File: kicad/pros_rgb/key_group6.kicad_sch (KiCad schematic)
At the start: 16 parts

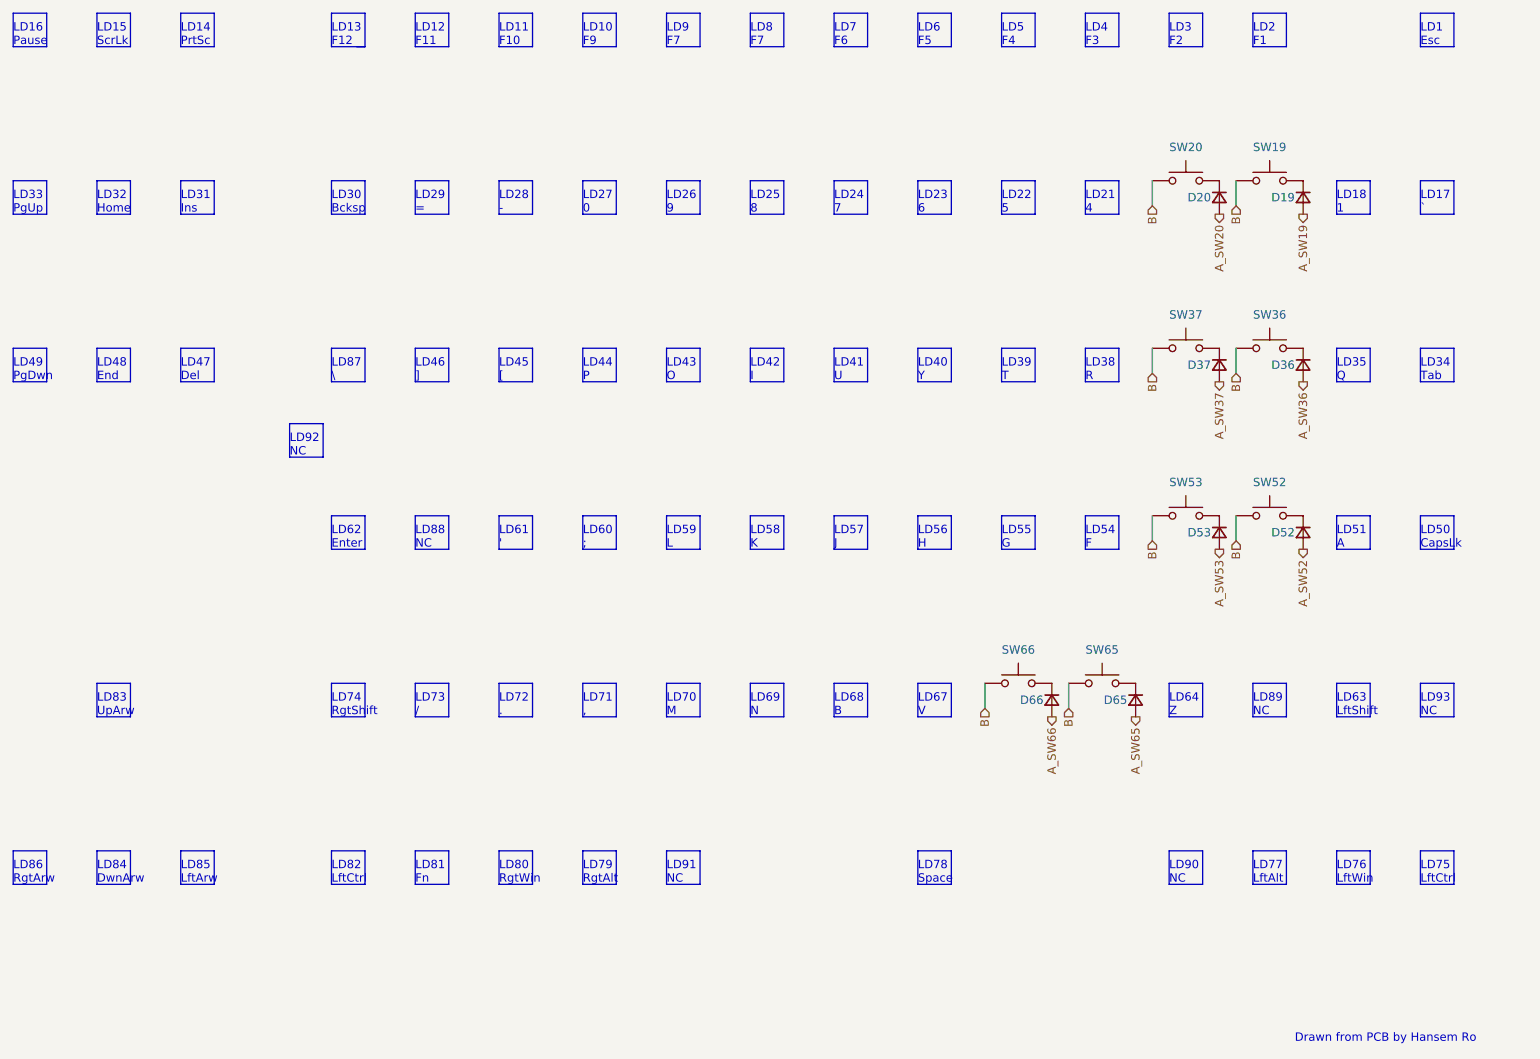
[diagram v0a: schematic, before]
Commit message: kicad/pros_rgb: update key groupings
These new groupings are based off ordering in firmware:
https://github.com/hansemro/pok3r_re_firmware/blob/4b68aa4baf7d28dc8dbf8eebcb1fdb59e7bcd629/disassemble/cmprosrgb/v122/cmprosrgb_v122.txt#L14599-L14629
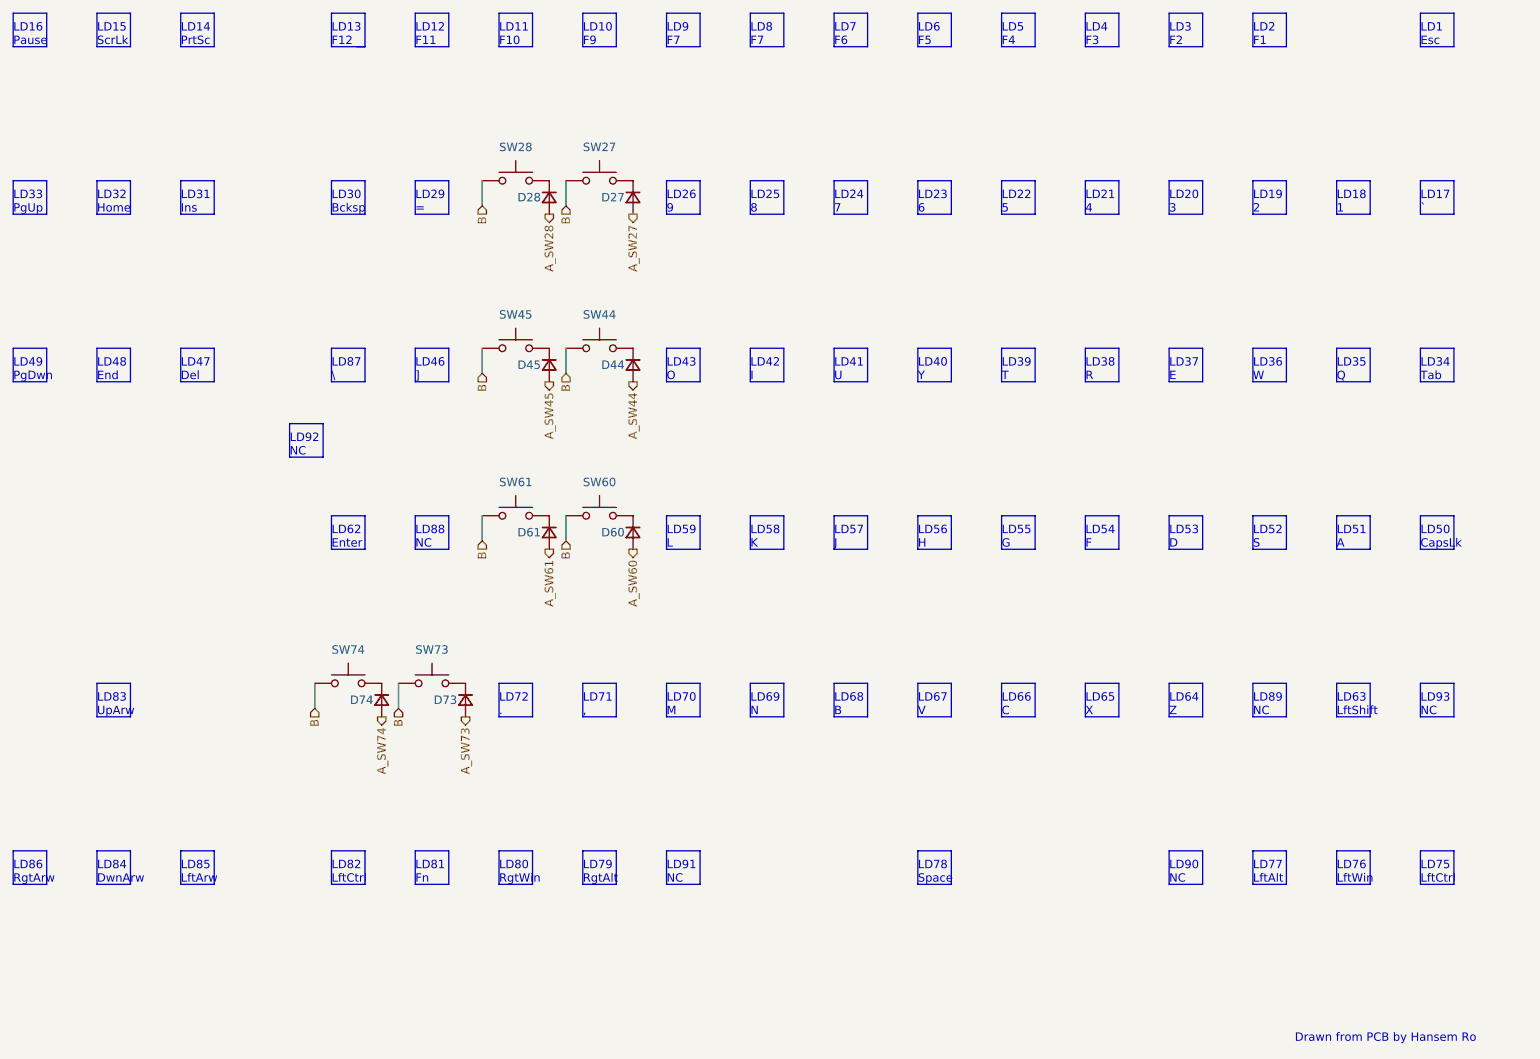
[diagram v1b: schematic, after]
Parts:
- removed D19, D20, D36, D37, D52, D53, D65, D66: ~, symbol Device:D_Small
- removed SW19, SW20, SW36, SW37, SW52, SW53, SW65, SW66: ~, symbol Switch:SW_Push
- added D27, D28, D44, D45, D60, D61, D73, D74: (no value), symbol Device:D_Small
- added SW27, SW28, SW44, SW45, SW60, SW61, SW73, SW74: (no value), symbol Switch:SW_Push
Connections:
- net B: now also SW27.1, SW28.1, SW44.1, SW45.1, SW60.1, SW61.1, SW73.1, SW74.1
- new net: D28.1 (K), SW28.2
- new net: D74.1 (K), SW74.2
- new net: D44.1 (K), SW44.2
- new net: D61.1 (K), SW61.2
- new net: D45.1 (K), SW45.2
- new net: D73.1 (K), SW73.2
- new net: D60.1 (K), SW60.2
- new net: D27.1 (K), SW27.2
- new net A_SW27: D27.2 (A)
- new net A_SW28: D28.2 (A)
- new net A_SW44: D44.2 (A)
- new net A_SW45: D45.2 (A)
- new net A_SW60: D60.2 (A)
- new net A_SW61: D61.2 (A)
- new net A_SW73: D73.2 (A)
- new net A_SW74: D74.2 (A)
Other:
- note added: "LD19 2"
- note added: "LD20 3"
- note added: "LD36 W"
- note added: "LD37 E"
- note added: "LD52 S"
- note added: "LD53 D"
- note added: "LD65 X"
- note added: "LD66 C"
- note removed: "LD27 0"
- note removed: "LD28 -"
- note removed: "LD44 P"
- note removed: "LD45 ["
- note removed: "LD60 ;"
- note removed: "LD61 '"
- note removed: "LD73 /"
- note removed: "LD74 RgtShift"

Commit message: kicad/pros_rgb: mark as Rev. B
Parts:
- D27, D28, D44, D45, D60, D61, D73, D74, SW27, SW28, SW44, SW45, SW60, SW61, SW73, SW74: value (none) -> ~
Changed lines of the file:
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@@
     (in_bom yes) (on_board yes)
     (property "Reference" "SW28" (id 0) (at 134.62 44.45 0))
-    (property "Value" "" (id 1) (at 134.62 44.45 0))
+    (property "Value" "~" (id 1) (at 134.62 44.45 0))
     (property "Footprint" "" (id 2) (at 134.62 44.45 0)
       (effects (font (size 1.27 1.27)) hide)
@@
     (in_bom yes) (on_board yes)
     (property "Reference" "SW74" (id 0) (at 109.22 120.65 0))
-    (property "Value" "" (id 1) (at 109.22 120.65 0))
+    (property "Value" "~" (id 1) (at 109.22 120.65 0))
     (property "Footprint" "" (id 2) (at 109.22 120.65 0)
       (effects (font (size 1.27 1.27)) hide)
@@
     (in_bom yes) (on_board yes)
     (property "Reference" "SW44" (id 0) (at 147.32 69.85 0))
-    (property "Value" "" (id 1) (at 147.32 69.85 0))
+    (property "Value" "~" (id 1) (at 147.32 69.85 0))
     (property "Footprint" "" (id 2) (at 147.32 69.85 0)
       (effects (font (size 1.27 1.27)) hide)
@@
       (effects (font (size 1.27 1.27)) (justify right))
     )
-    (property "Value" "" (id 1) (at 142.24 104.1399 90)
+    (property "Value" "~" (id 1) (at 142.24 104.1399 90)
       (effects (font (size 1.27 1.27)) (justify left))
     )
@@
       (effects (font (size 1.27 1.27)) (justify right))
     )
-    (property "Value" "" (id 1) (at 142.24 78.7399 90)
+    (property "Value" "~" (id 1) (at 142.24 78.7399 90)
       (effects (font (size 1.27 1.27)) (justify left))
     )
@@
       (effects (font (size 1.27 1.27)) (justify right))
     )
-    (property "Value" "" (id 1) (at 129.54 129.5399 90)
+    (property "Value" "~" (id 1) (at 129.54 129.5399 90)
       (effects (font (size 1.27 1.27)) (justify left))
     )
@@
     (in_bom yes) (on_board yes)
     (property "Reference" "SW73" (id 0) (at 121.92 120.65 0))
-    (property "Value" "" (id 1) (at 121.92 120.65 0))
+    (property "Value" "~" (id 1) (at 121.92 120.65 0))
     (property "Footprint" "" (id 2) (at 121.92 120.65 0)
       (effects (font (size 1.27 1.27)) hide)
@@
       (effects (font (size 1.27 1.27)) (justify right))
     )
-    (property "Value" "" (id 1) (at 116.84 129.5399 90)
+    (property "Value" "~" (id 1) (at 116.84 129.5399 90)
       (effects (font (size 1.27 1.27)) (justify left))
     )
@@
     (in_bom yes) (on_board yes)
     (property "Reference" "SW61" (id 0) (at 134.62 95.25 0))
-    (property "Value" "" (id 1) (at 134.62 95.25 0))
+    (property "Value" "~" (id 1) (at 134.62 95.25 0))
     (property "Footprint" "" (id 2) (at 134.62 95.25 0)
       (effects (font (size 1.27 1.27)) hide)
@@
     (in_bom yes) (on_board yes)
     (property "Reference" "SW45" (id 0) (at 134.62 69.85 0))
-    (property "Value" "" (id 1) (at 134.62 69.85 0))
+    (property "Value" "~" (id 1) (at 134.62 69.85 0))
     (property "Footprint" "" (id 2) (at 134.62 69.85 0)
       (effects (font (size 1.27 1.27)) hide)
@@
       (effects (font (size 1.27 1.27)) (justify right))
     )
-    (property "Value" "" (id 1) (at 142.24 53.3399 90)
+    (property "Value" "~" (id 1) (at 142.24 53.3399 90)
       (effects (font (size 1.27 1.27)) (justify left))
     )
@@
       (effects (font (size 1.27 1.27)) (justify right))
     )
-    (property "Value" "" (id 1) (at 154.94 78.7399 90)
+    (property "Value" "~" (id 1) (at 154.94 78.7399 90)
       (effects (font (size 1.27 1.27)) (justify left))
     )
@@
       (effects (font (size 1.27 1.27)) (justify right))
     )
-    (property "Value" "" (id 1) (at 154.94 104.1399 90)
+    (property "Value" "~" (id 1) (at 154.94 104.1399 90)
       (effects (font (size 1.27 1.27)) (justify left))
     )
@@
       (effects (font (size 1.27 1.27)) (justify right))
     )
-    (property "Value" "" (id 1) (at 154.94 53.3399 90)
+    (property "Value" "~" (id 1) (at 154.94 53.3399 90)
       (effects (font (size 1.27 1.27)) (justify left))
     )
@@
     (in_bom yes) (on_board yes)
     (property "Reference" "SW27" (id 0) (at 147.32 44.45 0))
-    (property "Value" "" (id 1) (at 147.32 44.45 0))
+    (property "Value" "~" (id 1) (at 147.32 44.45 0))
     (property "Footprint" "" (id 2) (at 147.32 44.45 0)
       (effects (font (size 1.27 1.27)) hide)
@@
     (in_bom yes) (on_board yes)
     (property "Reference" "SW60" (id 0) (at 147.32 95.25 0))
-    (property "Value" "" (id 1) (at 147.32 95.25 0))
+    (property "Value" "~" (id 1) (at 147.32 95.25 0))
     (property "Footprint" "" (id 2) (at 147.32 95.25 0)
       (effects (font (size 1.27 1.27)) hide)

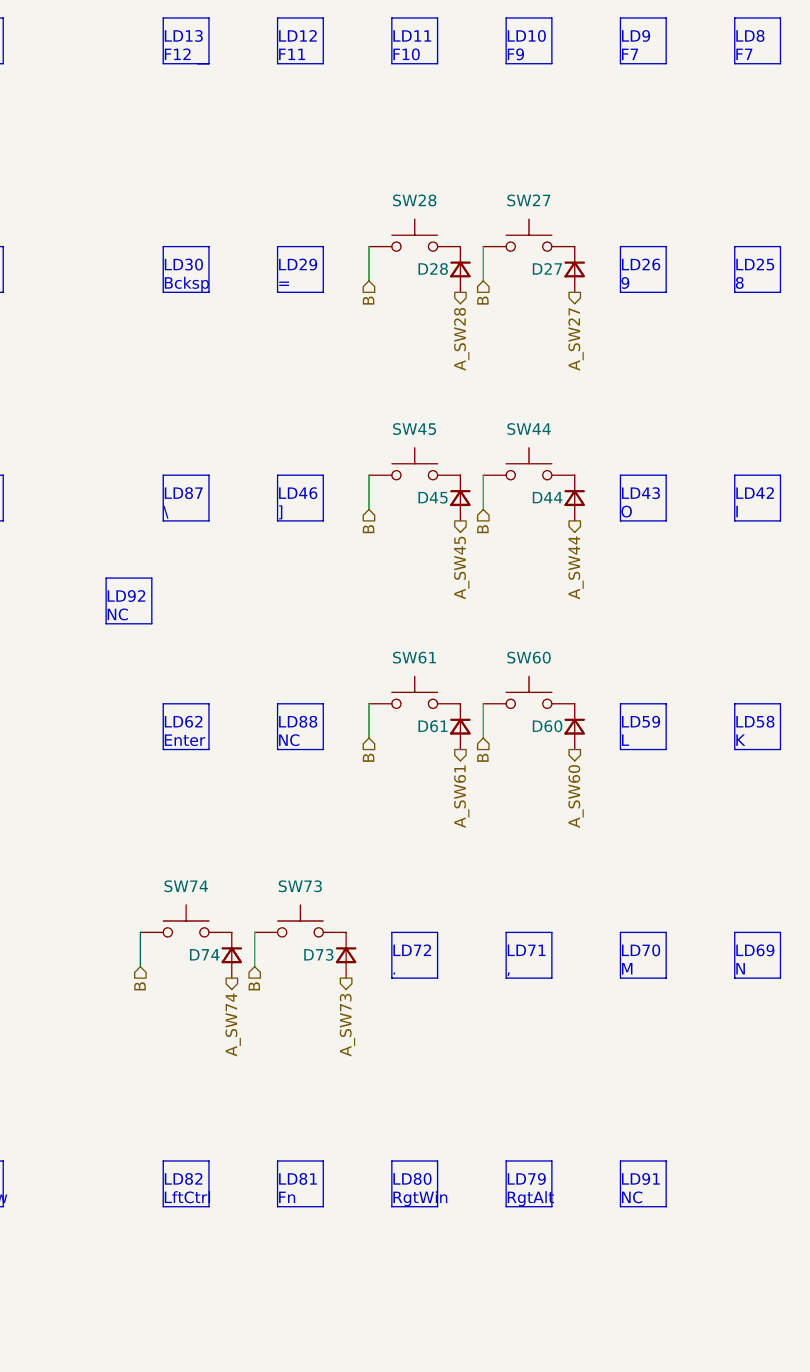
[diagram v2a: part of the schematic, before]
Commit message: kicad/pros_rgb: fix typos
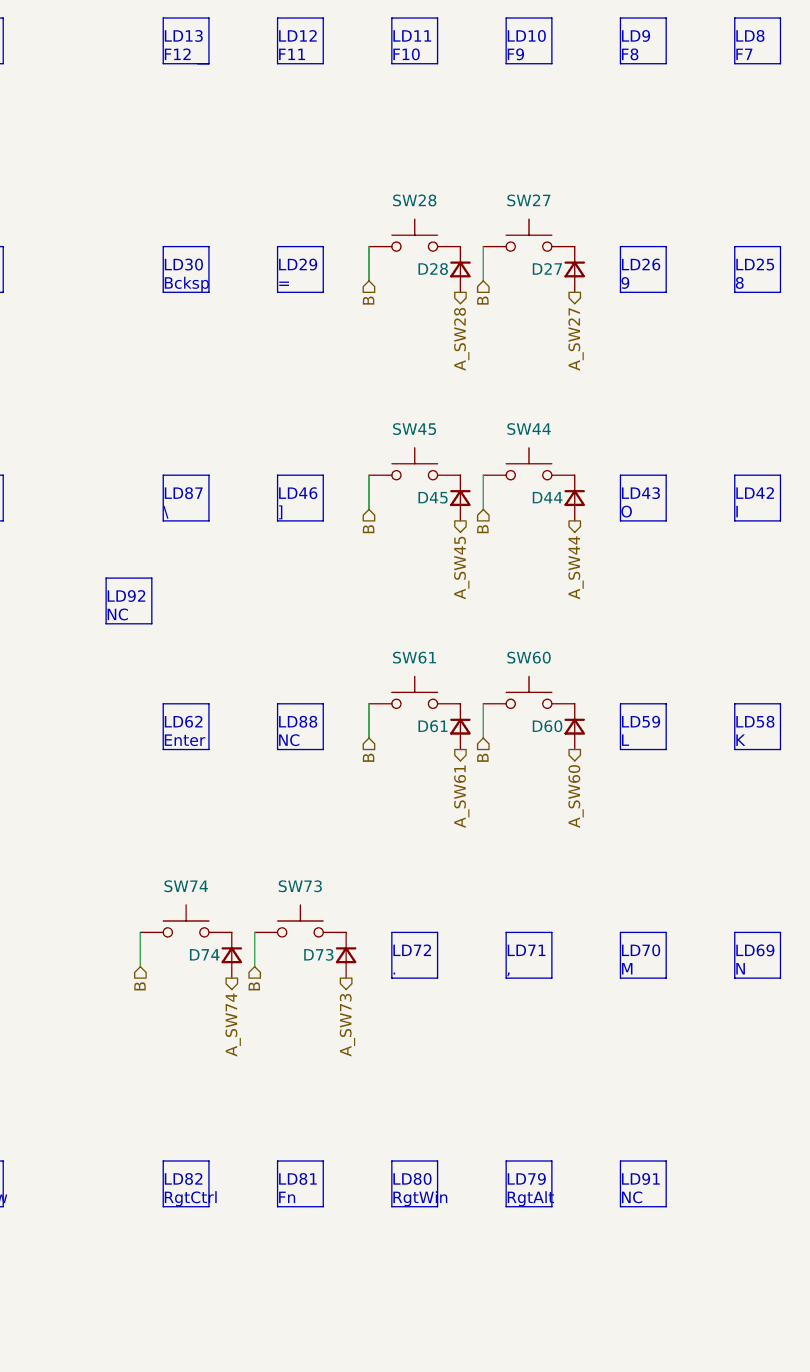
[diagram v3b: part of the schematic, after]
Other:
- note added: "LD82 RgtCtrl"
- note added: "LD9 F8"
- note removed: "LD82 LftCtrl"
- note removed: "LD9 F7"
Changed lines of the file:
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@@
     (effects (font (size 1.27 1.27)) (justify left bottom))
   )
-  (text "LD9\nF7" (at 157.48 29.21 0)
+  (text "LD9\nF8" (at 157.48 29.21 0)
     (effects (font (size 1.27 1.27)) (justify left bottom))
   )
@@
     (effects (font (size 1.27 1.27)) (justify left bottom))
   )
-  (text "LD82\nLftCtrl" (at 106.68 156.21 0)
+  (text "LD82\nRgtCtrl" (at 106.68 156.21 0)
     (effects (font (size 1.27 1.27)) (justify left bottom))
   )
